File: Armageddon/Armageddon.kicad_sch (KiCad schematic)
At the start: 10 parts, among them J1 XT60PW-M, U2 PTPS16850VMAR

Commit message: Output Capacitances
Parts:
- added C5: 100pF, Capacitor_SMD:C_0603_1608Metric_Pad1.08x0.95mm_HandSolder, symbol Device:C
- added C6: 100nF/50V, Capacitor_SMD:C_0805_2012Metric, symbol Device:C_Small
- added C7: 22uF/50V, Capacitor_SMD:C_2220_5750Metric_Pad1.97x5.40mm_HandSolder, symbol Device:C
- added D2: SMAJ28A, Diode_SMD:D_SMA, symbol Diode:SMAJ28A
- added J2: 530470610, Connector_Molex:Molex_PicoBlade_53047-0610_1x06_P1.25mm_Vertical, symbol Molex 530470610:530470610
- added R4: 330K, Resistor_SMD:R_0603_1608Metric_Pad0.98x0.95mm_HandSolder, symbol Device:R
- added R5: 720K, Resistor_SMD:R_0603_1608Metric_Pad0.98x0.95mm_HandSolder, symbol Device:R
- added R6: 30K, Resistor_SMD:R_0603_1608Metric_Pad0.98x0.95mm_HandSolder, symbol Device:R
- added TP1: TestPoint_Alt, symbol Connector:TestPoint_Alt
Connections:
- net GND: now also C6.2, C7.2, D2.2 (A2), R4.2, R6.2
- net at C1.1, C2.1, D1.1 (A1)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: now also R5.1
- net PWR PB-: now reaches C4.1, R3.1, U2.16 (EN_UVLO)
- net PWR PB-: now also C5.2, J2.2; no longer R2.2
- net at U2.18 (OVP): now also R5.2, R6.1
- net at U2.20 (SWEN): now also TP1.1
- net at U2.6 (SFT_SEL): now also R4.1
- net +24V: now reaches U2.7 (OUT)
- net +24V: now also U2.8 (OUT), C6.1, C7.1, D2.1 (A1)
- new net PWR PB+: C5.1, J2.1, R2.2
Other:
- note added: "Iocp * 1.5"
- note added: "OVPR: 30V"
- moved on the sheet: C1, C2, C3, C4, D1, J1, R1, R2, R3, U2

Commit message: Added Good and Fault LEDS
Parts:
- added R7, R8: 1K, Resistor_SMD:R_0603_1608Metric_Pad0.98x0.95mm_HandSolder, symbol Device:R
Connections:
- net GND: now also J2.6
- net R_LED_A: now reaches J2.3
- net R_LED_A: now also R7.2
- net PFault: now reaches J2.4
- net PFault: now also U2.13 (FLT_N)
- net Pgood: now reaches J2.5
- net Pgood: now also U2.19 (PGOOD), R8.2
- new net +5V: R7.1, R8.1
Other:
- note added: "To G LED A"
- note added: "To G LED K"
- note added: "To R LED K"
- moved on the sheet: J2

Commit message: adding zener for FAULT/PGOOD
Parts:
- added C8: 100pF, Capacitor_SMD:C_0603_1608Metric_Pad1.08x0.95mm_HandSolder, symbol Device:C
- added CR1: MMSZ5231B-7-F, SOD123_DIO, symbol MMSZ5231B_7_F:MMSZ5231B-7-F
- added R9: 3K9, Resistor_SMD:R_0603_1608Metric_Pad0.98x0.95mm_HandSolder, symbol Device:R
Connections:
- net GND: now also C8.2, CR1.2
- net 24V Vin: now reaches C1.1, C2.1, D1.1 (A1), J1.1 (P), R1.1, R2.1, R5.1, U2.10 (IN), U2.22 (IN), U2.23 (IN), U2.24 (IN)
- net 24V Vin: now also R9.1
- net at R5.2, R6.1, U2.18 (OVP): now also C8.1
- net +5V renamed +5VL
- net +5VL: now also CR1.1, R9.2

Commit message: Setting ITimer Pin
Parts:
- added C10: 100pF, Capacitor_SMD:C_0603_1608Metric_Pad1.08x0.95mm_HandSolder, symbol Device:C
- added C11, C13: 22pF, Capacitor_SMD:C_0603_1608Metric_Pad1.08x0.95mm_HandSolder, symbol Device:C
- added C12: 4.7nF/50V, Capacitor_SMD:C_0603_1608Metric_Pad1.08x0.95mm_HandSolder, symbol Device:C
- added C9: 47nF/50V, Capacitor_SMD:C_0603_1608Metric_Pad1.08x0.95mm_HandSolder, symbol Device:C
- added R10: 40.2K/0.1%, Resistor_SMD:R_0603_1608Metric_Pad0.98x0.95mm_HandSolder, symbol Device:R
- added R11: 3.92K/0.1%, Resistor_SMD:R_0603_1608Metric_Pad0.98x0.95mm_HandSolder, symbol Device:R
- added TP2: TestPoint_Alt, symbol Connector:TestPoint_Alt
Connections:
- net GND: now also U2.5 (GND), C10.2, C11.2, C12.2, C13.2, C9.2, R10.2, R11.2
- net at U2.14 (ITIMER): now also C12.1
- net at U2.15 (TEMP): now also C13.1, TP2.1
- net at U2.2 (IMON): now also C11.1, R11.1
- net at U2.3 (IREF): now also C10.1, R10.1
- net at U2.4 (dVdT): now also C9.1
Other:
- note added: "IOCP: 15A"
- moved on the sheet: C1, C2, C3, C4, C5, C6, C7, C8, CR1, D1, D2, J1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

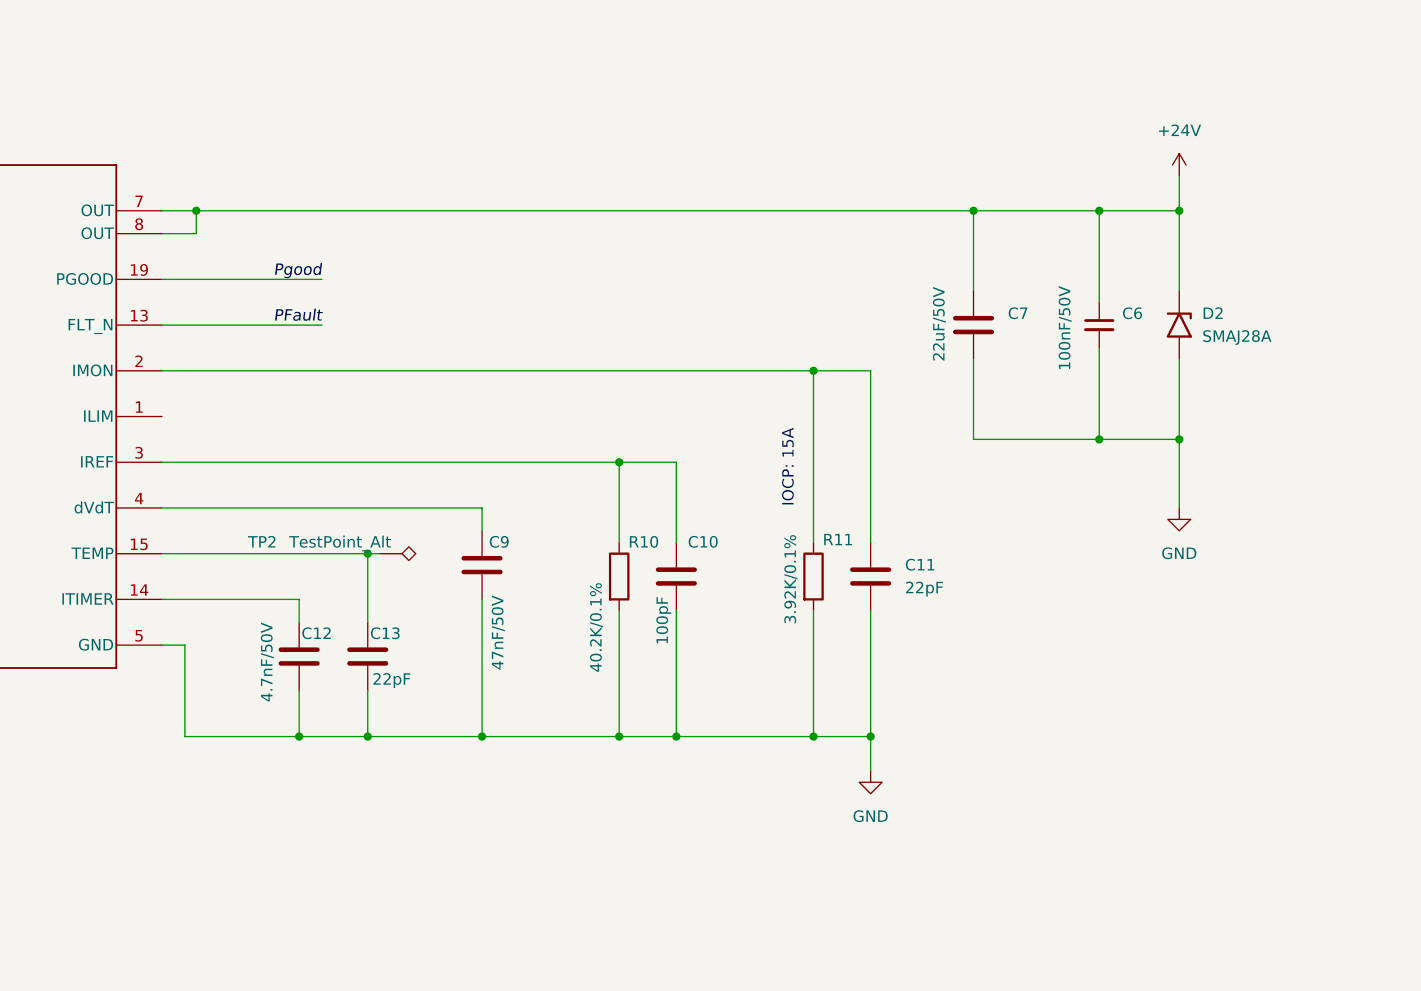
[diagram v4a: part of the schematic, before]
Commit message: Finishing the Efuse
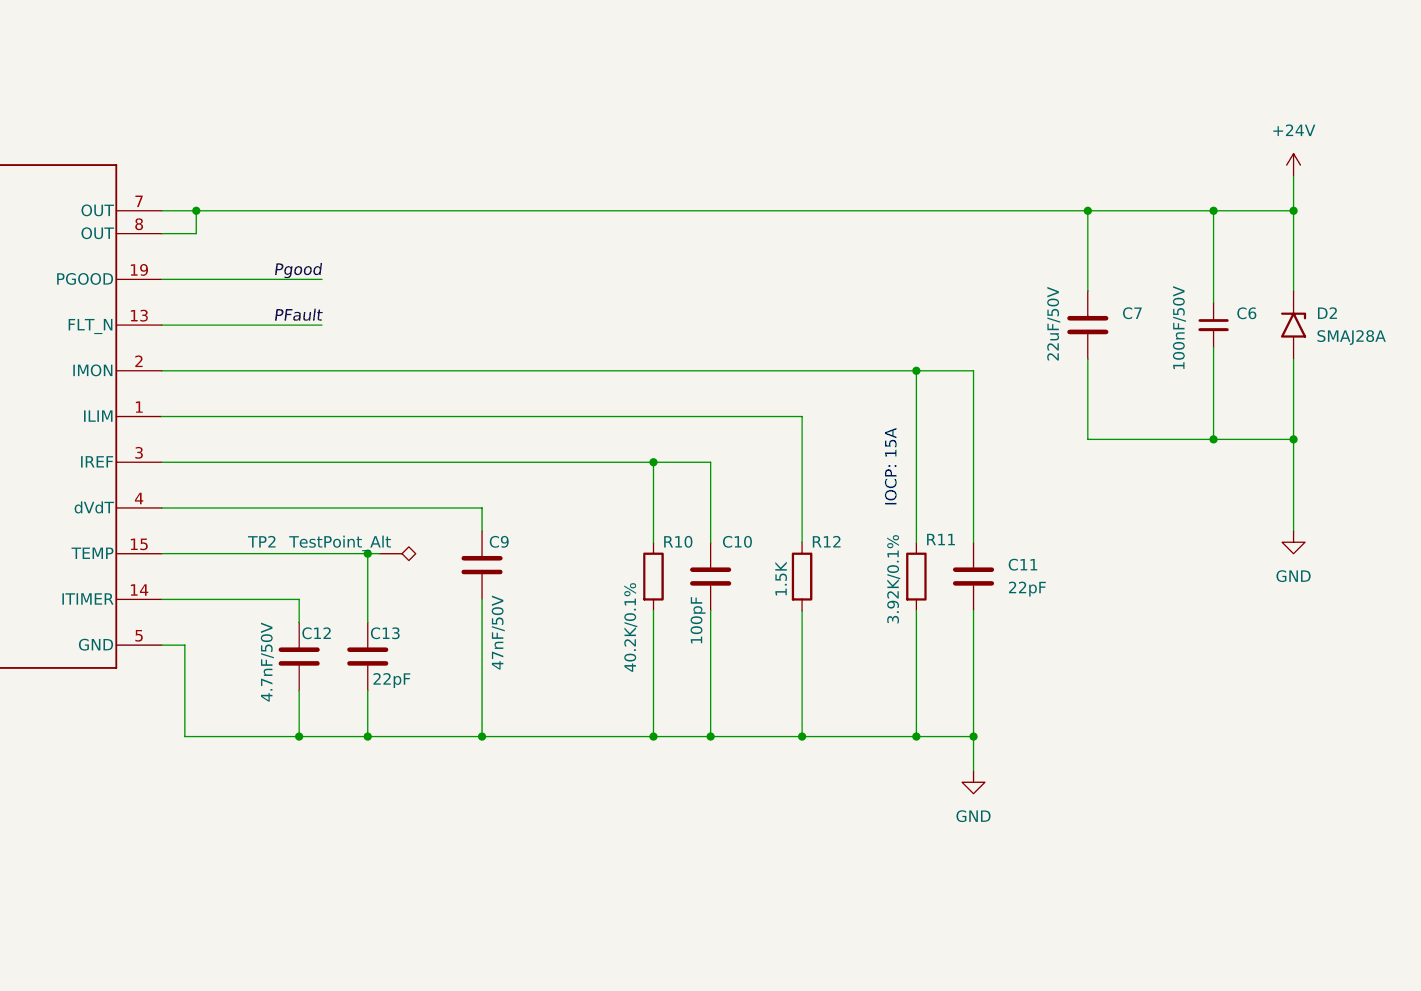
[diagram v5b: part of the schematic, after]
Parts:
- added R12: 1.5K, Resistor_SMD:R_0603_1608Metric_Pad0.98x0.95mm_HandSolder, symbol Device:R
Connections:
- net GND: now also R12.2
- net at U2.1 (ILIM): now also R12.1
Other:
- moved on the sheet: C10, C11, C6, C7, D2, R10, R11

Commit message: Removing EFUSE
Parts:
- removed C1: 22uF/50V, A768EB226M1HLAE048:CAPAE660X600N, symbol A768EB226M1HLAE048:A768EB226M1HLAE048
- removed C10, C4, C5, C8: 100pF, Capacitor_SMD:C_0603_1608Metric_Pad1.08x0.95mm_HandSolder, symbol Device:C
- removed C11, C13: 22pF, Capacitor_SMD:C_0603_1608Metric_Pad1.08x0.95mm_HandSolder, symbol Device:C
- removed C12: 4.7nF/50V, Capacitor_SMD:C_0603_1608Metric_Pad1.08x0.95mm_HandSolder, symbol Device:C
- removed C2, C6: 100nF/50V, Capacitor_SMD:C_0805_2012Metric, symbol Device:C_Small
- removed C3: 220nF/50V, Capacitor_SMD:C_0805_2012Metric, symbol Device:C_Small
- removed C7: 22uF/50V, Capacitor_SMD:C_2220_5750Metric_Pad1.97x5.40mm_HandSolder, symbol Device:C
- removed C9: 47nF/50V, Capacitor_SMD:C_0603_1608Metric_Pad1.08x0.95mm_HandSolder, symbol Device:C
- removed CR1: MMSZ5231B-7-F, SOD123_DIO, symbol MMSZ5231B_7_F:MMSZ5231B-7-F
- removed D1, D2: SMAJ28A, Diode_SMD:D_SMA, symbol Diode:SMAJ28A
- removed J1: XT60PW-M, XT60PW-M:AMASS_XT60PW-M, symbol XT60PW-M:XT60PW-M
- removed J2: 530470610, Connector_Molex:Molex_PicoBlade_53047-0610_1x06_P1.25mm_Vertical, symbol Molex 530470610:530470610
- removed R1: 150R, Resistor_SMD:R_0805_2012Metric, symbol Device:R
- removed R10: 40.2K/0.1%, Resistor_SMD:R_0603_1608Metric_Pad0.98x0.95mm_HandSolder, symbol Device:R
- removed R11: 3.92K/0.1%, Resistor_SMD:R_0603_1608Metric_Pad0.98x0.95mm_HandSolder, symbol Device:R
- removed R12: 1.5K, Resistor_SMD:R_0603_1608Metric_Pad0.98x0.95mm_HandSolder, symbol Device:R
- removed R2: 750K, Resistor_SMD:R_0603_1608Metric_Pad0.98x0.95mm_HandSolder, symbol Device:R
- removed R3: 100K, Resistor_SMD:R_0603_1608Metric_Pad0.98x0.95mm_HandSolder, symbol Device:R
- removed R4: 330K, Resistor_SMD:R_0603_1608Metric_Pad0.98x0.95mm_HandSolder, symbol Device:R
- removed R5: 720K, Resistor_SMD:R_0603_1608Metric_Pad0.98x0.95mm_HandSolder, symbol Device:R
- removed R6: 30K, Resistor_SMD:R_0603_1608Metric_Pad0.98x0.95mm_HandSolder, symbol Device:R
- removed R7, R8: 1K, Resistor_SMD:R_0603_1608Metric_Pad0.98x0.95mm_HandSolder, symbol Device:R
- removed R9: 3K9, Resistor_SMD:R_0603_1608Metric_Pad0.98x0.95mm_HandSolder, symbol Device:R
- removed TP1, TP2: TestPoint_Alt, symbol Connector:TestPoint_Alt
- removed U2: PTPS16850VMAR, VMA0023A-MFG, symbol TPS16850VMAR:PTPS16850VMAR
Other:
- note removed: "(24V/20A)"
- note removed: "24V in + EFuse"
- note removed: "IOCP: 15A"
- note removed: "Iocp * 1.5"
- note removed: "OVPR: 30V"
- note removed: "To G LED A"
- note removed: "To G LED K"
- note removed: "To R LED K"
- note removed: "UVLO 10V"

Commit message: Added 5V Rail
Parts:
- added C1: 47uF/50V, C_870135775004:WCAP-PTHT_10X12.5_DXL_, symbol Device:C_Polarized
- added C2, C4: 10uF/50V, Capacitor_SMD:C_1206_3216Metric_Pad1.33x1.80mm_HandSolder, symbol Device:C_Small
- added C3, C5: 100nF/50V, Capacitor_SMD:C_0805_2012Metric_Pad1.18x1.45mm_HandSolder, symbol Device:C_Small
- added C6: 22pF/50V, Capacitor_SMD:C_0805_2012Metric_Pad1.18x1.45mm_HandSolder, symbol Device:C_Small
- added C7: 100uF, Capacitor_SMD:C_1206_3216Metric_Pad1.33x1.80mm_HandSolder, symbol Device:C_Small
- added C8, C9: 47uF, Capacitor_SMD:C_1206_3216Metric_Pad1.33x1.80mm_HandSolder, symbol Device:C_Small
- added D1: SMAJ30A, Diode_SMD:D_SMA, symbol Diode:SMAJ30A
- added J1: XT60PW-M, XT60PW-M:AMASS_XT60PW-M, symbol XT60PW-M:XT60PW-M
- added J2: 530470610, CONN06_530470610_MOL, symbol Molex 530470610:530470610
- added R1: 4K7, Resistor_SMD:R_1206_3216Metric_Pad1.30x1.75mm_HandSolder, symbol Device:R
- added R2: 187K, Resistor_SMD:R_0603_1608Metric_Pad0.98x0.95mm_HandSolder, symbol Device:R
- added R3: 49.9K, Resistor_SMD:R_0603_1608Metric_Pad0.98x0.95mm_HandSolder, symbol Device:R
- added R4, R6: 100K, Resistor_SMD:R_0603_1608Metric_Pad0.98x0.95mm_HandSolder, symbol Device:R
- added R5: 15.8K, Resistor_SMD:R_0603_1608Metric_Pad0.98x0.95mm_HandSolder, symbol Device:R
- added R7: 24.9K, Resistor_SMD:R_0603_1608Metric_Pad0.98x0.95mm_HandSolder, symbol Device:R
- added R8, R9: 470R, Resistor_SMD:R_0603_1608Metric_Pad0.98x0.95mm_HandSolder, symbol Device:R
- added U1: TLVM13610RDFR, RDF0022A-MFG, symbol TVLM13610:TLVM13610RDFR
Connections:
- new net: R2.2, R3.1, U1.17 (EN)
- new net: R4.2, U1.6 (VCC)
- new net: C6.2, R6.2, R7.1, U1.8 (FB)
- new net: C4.1, C5.1, U1.18 (VIN)
- new net: R5.1, U1.12 (RT)
- new net: U1.2 (RBOOT), U1.3 (CBOOT)
- new net +24V: C1.1, C2.1, C3.1, D1.1 (A1), J1.1 (P), R1.1, R2.1, U1.1 (VIN)
- new net +3V3: R9.1
- new net +5V: C6.1, C7.1, C8.1, C9.1, R6.1, R8.1, U1.10 (VOUT), U1.5 (VLDOIN), U1.9 (VOUT)
- new net 24VPLED: J2.1, R1.2
- new net 3V3PLED: J2.5, R9.2
- new net 5VGOOD: R4.1, U1.13 (PG)
- new net 5VPLED: J2.3, R8.2
- new net GND: C1.2, C2.2, C3.2, C4.2, C5.2, C7.2, C8.2, C9.2, D1.2 (A2), J1.2 (N), J1.SH1 (SHIELD), J1.SH2 (SHIELD), U1.19 (PGND), U1.20 (PGND)
- new net GNDS: J2.2, J2.4, J2.6, R3.2, R5.2, R7.2, U1.11 (AGND), U1.14 (AGND), U1.15 (AGND), U1.21 (AGND), U1.22 (AGND), U1.7 (AGND)
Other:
- note added: "5V 8A"
